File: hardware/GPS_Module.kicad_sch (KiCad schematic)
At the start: 1 part, among them U6 SAM-M8Q

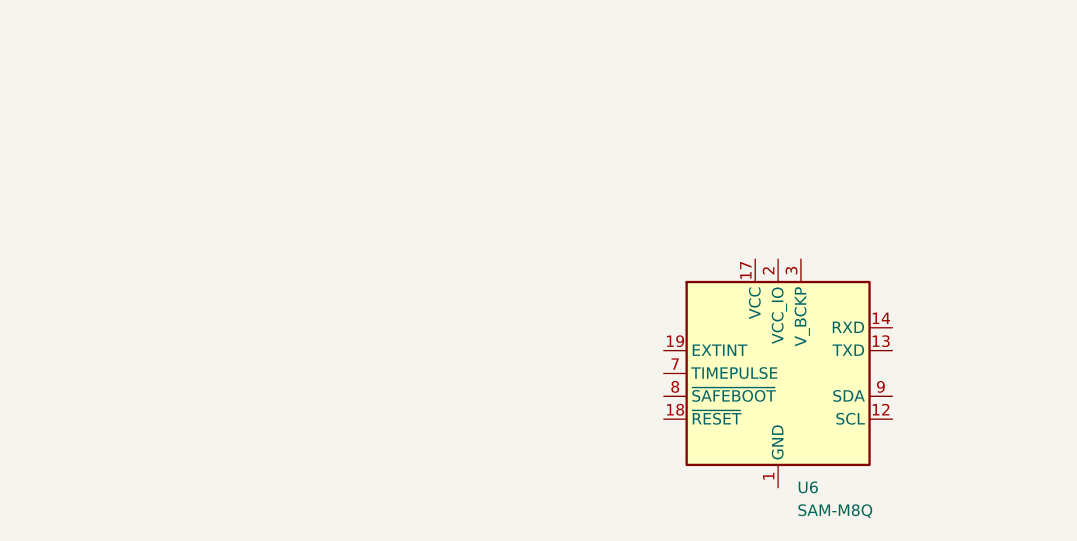
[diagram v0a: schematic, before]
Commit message: Main modules added + Com lines
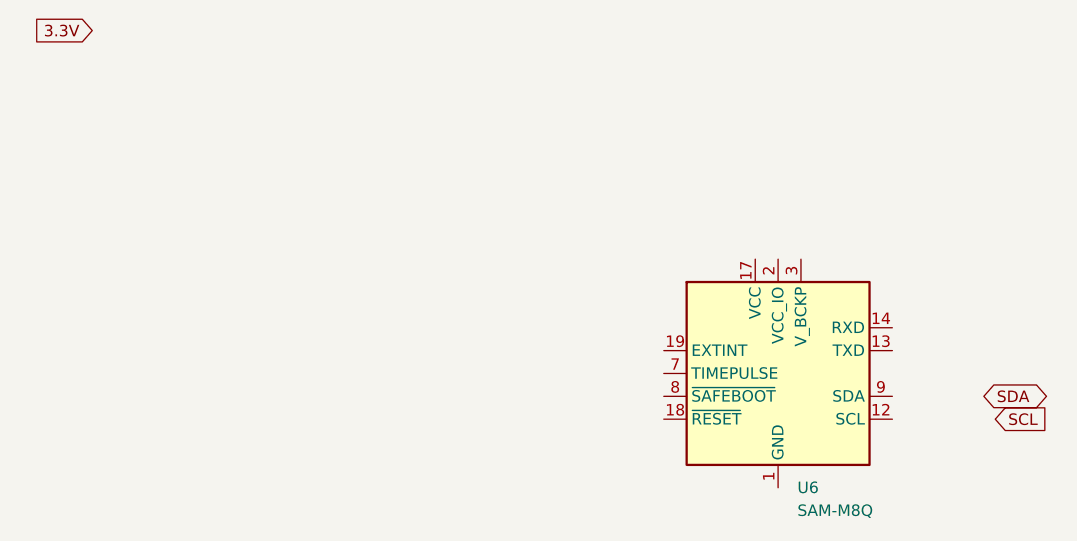
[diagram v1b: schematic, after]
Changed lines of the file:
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@@
 	(generator_version "9.0")
 	(paper "A4")
+	(global_label "3.3V"
+		(shape input)
+		(at 27.94 33.02 180)
+		(fields_autoplaced yes)
+		(effects
+			(font
+				(size 1.27 1.27)
+			)
+			(justify right)
+		)
+		(property "Intersheetrefs" "${INTERSHEET_REFS}"
+			(at 20.8424 33.02 0)
+			(effects
+				(font
+					(size 1.27 1.27)
+				)
+				(justify right)
+				(hide yes)
+			)
+		)
+	)
+	(global_label "SCL"
+		(shape input)
+		(at 128.27 76.2 0)
+		(fields_autoplaced yes)
+		(effects
+			(font
+				(size 1.27 1.27)
+			)
+			(justify left)
+		)
+		(property "Intersheetrefs" "${INTERSHEET_REFS}"
+			(at 134.7628 76.2 0)
+			(effects
+				(font
+					(size 1.27 1.27)
+				)
+				(justify left)
+				(hide yes)
+			)
+		)
+	)
+	(global_label "SDA"
+		(shape bidirectional)
+		(at 127 73.66 0)
+		(fields_autoplaced yes)
+		(effects
+			(font
+				(size 1.27 1.27)
+			)
+			(justify left)
+		)
+		(property "Intersheetrefs" "${INTERSHEET_REFS}"
+			(at 134.6646 73.66 0)
+			(effects
+				(font
+					(size 1.27 1.27)
+				)
+				(justify left)
+				(hide yes)
+			)
+		)
+	)
 	(symbol
 		(lib_id "RF_GPS:SAM-M8Q")

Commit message: GPS schematic + datasheet
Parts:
- added C10: 1µF, Capacitor_SMD:C_0603_1608Metric, symbol Device:C
- added D1: R_LED, LED_SMD:LED_0603_1608Metric, symbol Device:LED
- added J2, J3, J4: Conn_01x04_Pin, Connector_JST:JST_XA_B04B-XASK-1_1x04_P2.50mm_Vertical, symbol Connector:Conn_01x04_Pin
- added R13: 1k, Resistor_SMD:R_0603_1608Metric, symbol Device:R
- added R14, R15: 470, Resistor_SMD:R_0603_1608Metric, symbol Device:R
- added R8, R9: 22, Resistor_SMD:R_0603_1608Metric, symbol Device:R
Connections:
- net 3.3V: now also U6.17 (VCC), U6.2 (VCC_IO), C10.1, J2.1 (Pin_1), J3.1 (Pin_1)
- net SCL: now also J2.2 (Pin_2), R9.1
- net SDA: now also J2.3 (Pin_3), R8.2
- net GND: now reaches U6.1 (GND), U6.10 (GND), U6.11 (GND), U6.15 (GND), U6.16 (GND), U6.20 (GND), U6.4 (GND), U6.5 (GND), U6.6 (GND)
- net GND: now also C10.2, D1.1 (K), J2.4 (Pin_4), J3.4 (Pin_4)
- net at U6.12 (SCL): now also R9.2
- net at U6.13 (TXD): now also R15.2
- net at U6.14 (RXD): now also R14.1
- net ~{reset}: now reaches U6.18 (~{RESET})
- net ~{reset}: now also J4.4 (Pin_4)
- net EXTINT: now reaches U6.19 (EXTINT)
- net EXTINT: now also J4.1 (Pin_1)
- net TP: now reaches U6.7 (TIMEPULSE)
- net TP: now also J4.2 (Pin_2), R13.2
- net ~{safe}: now reaches U6.8 (~{SAFEBOOT})
- net ~{safe}: now also J4.3 (Pin_3)
- net at U6.9 (SDA): now also R8.1
- new net: D1.2 (A), R13.1
- new net RX_GPS: J3.3 (Pin_3), R14.2
- new net TX_GPS: J3.2 (Pin_2), R15.1
- no-connect marks 0 -> 1
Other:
- moved on the sheet: U6

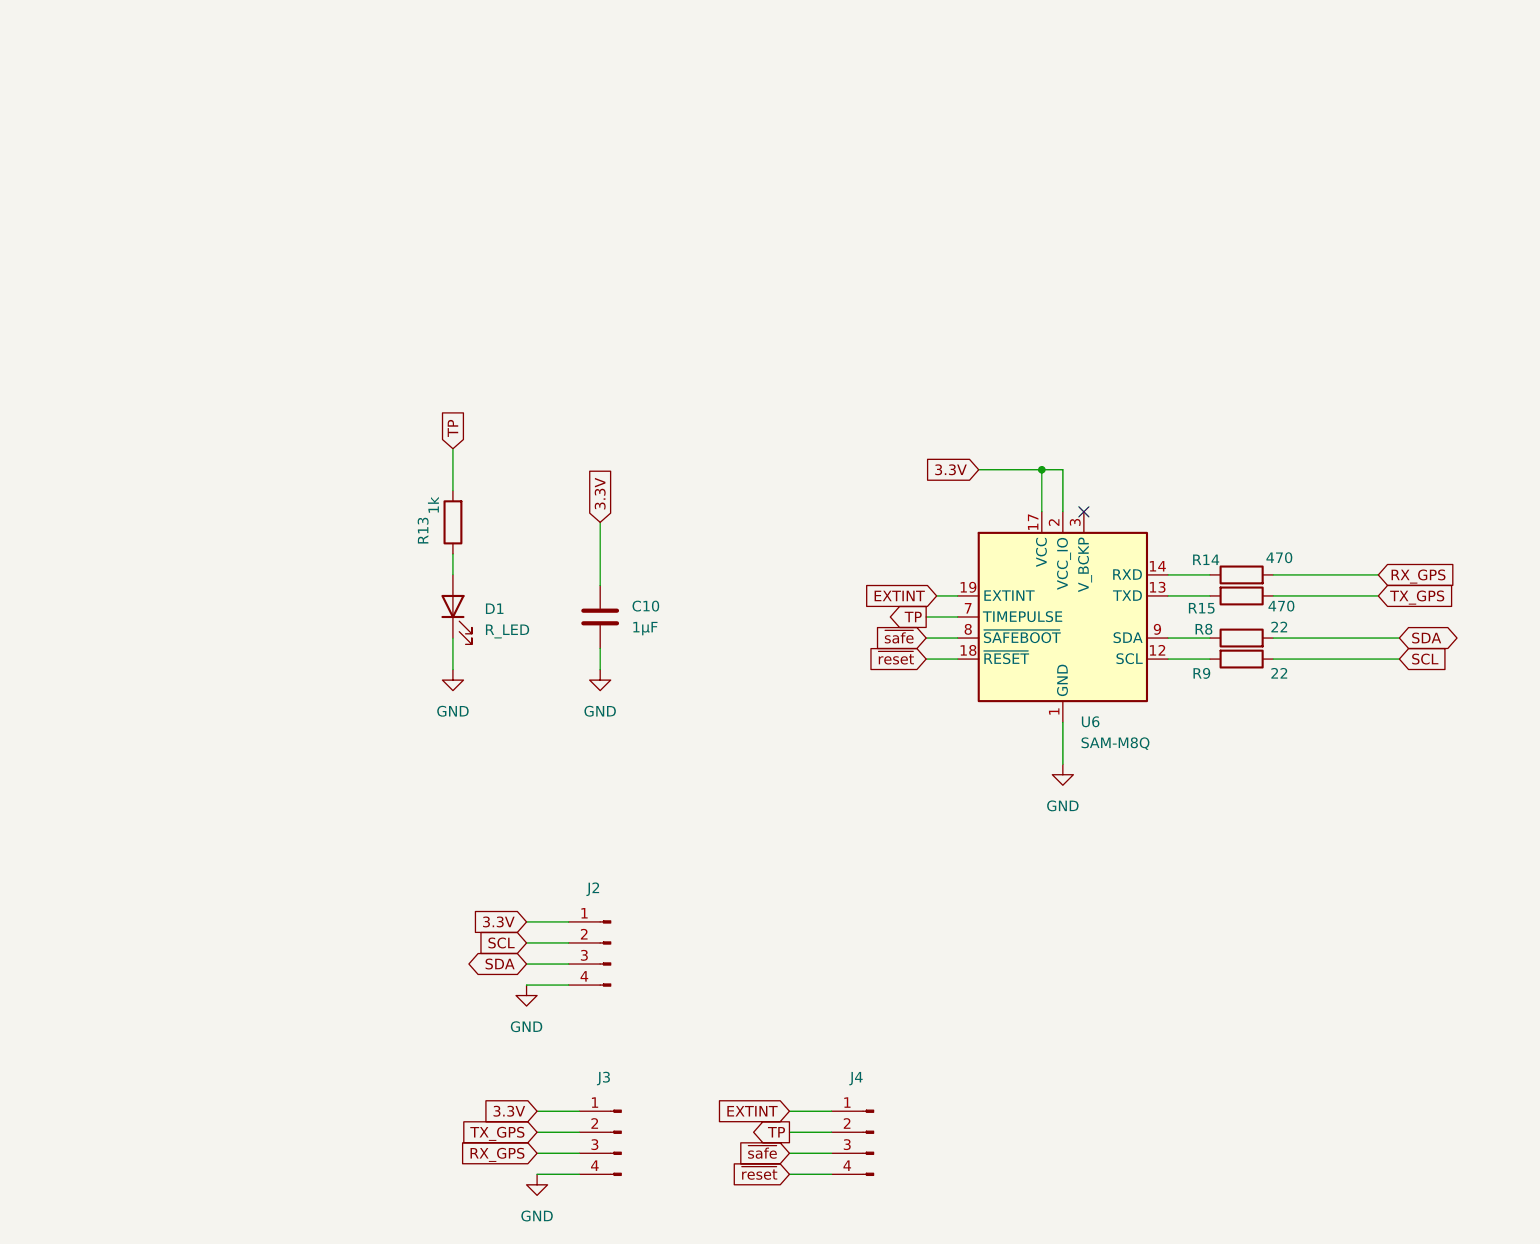
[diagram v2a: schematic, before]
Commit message: ESL protection modification with usblc6 2sc6
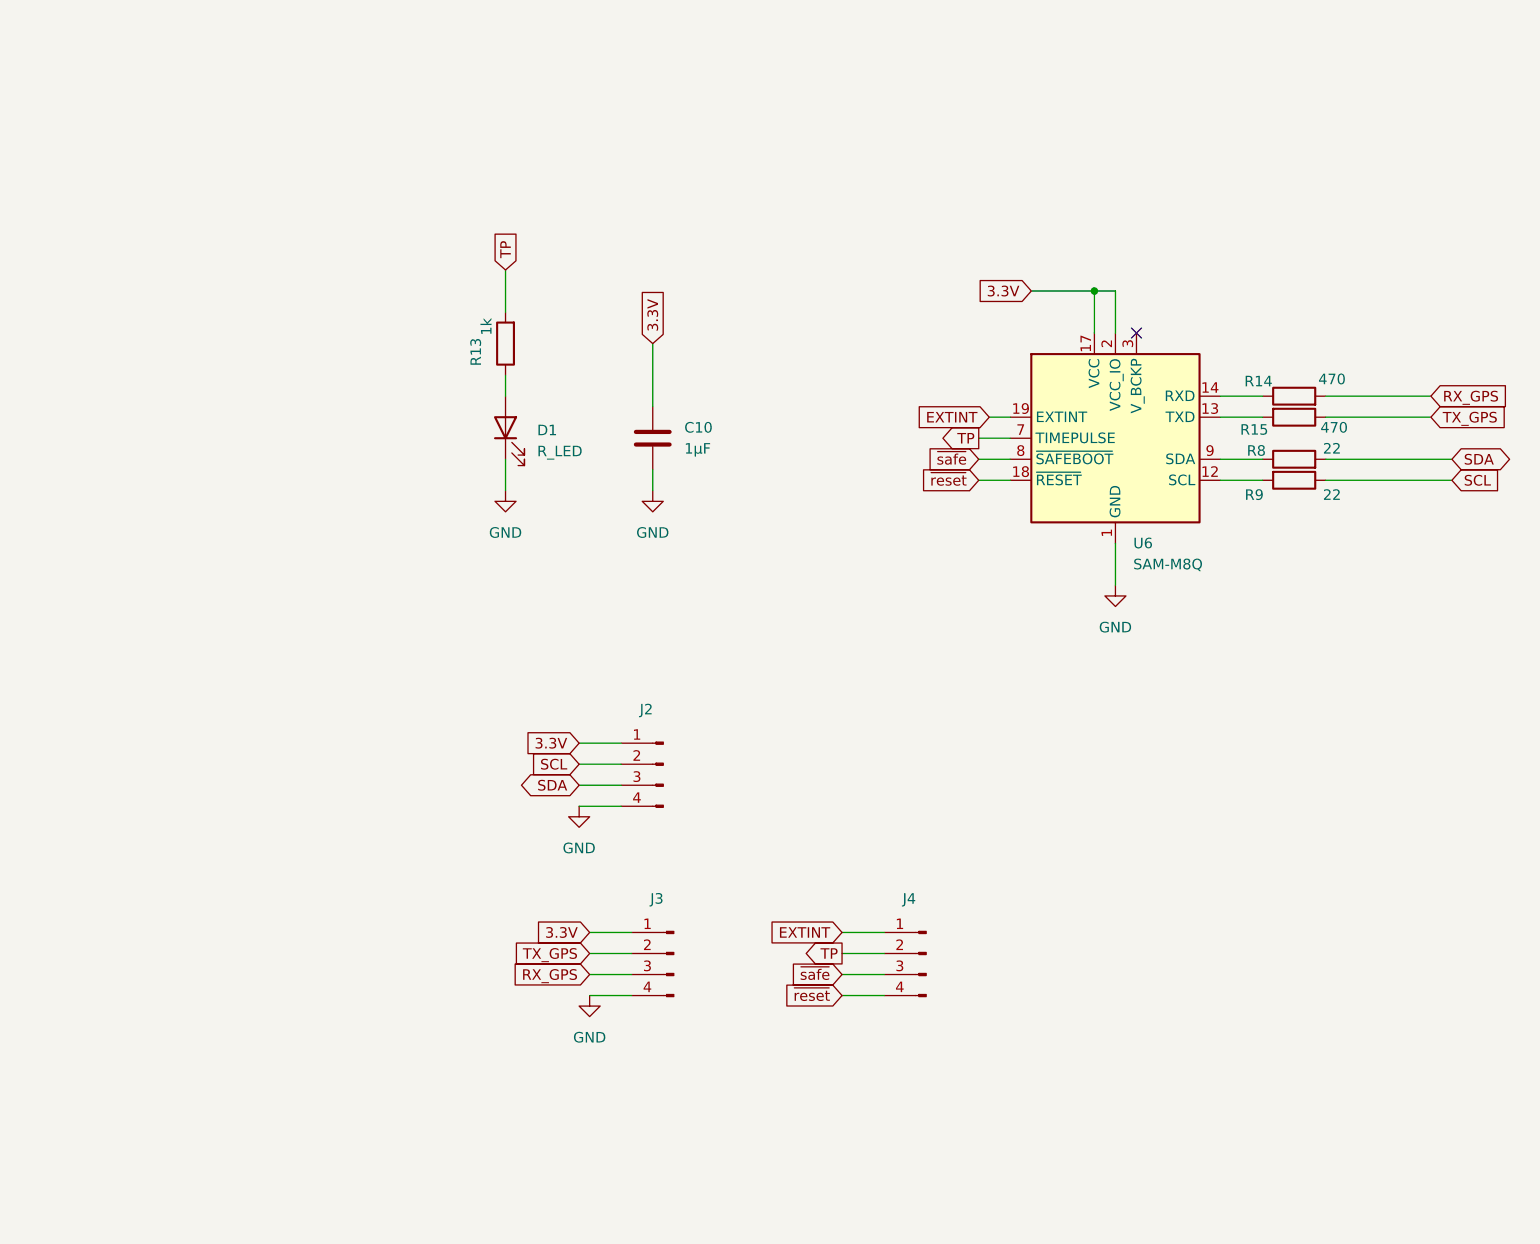
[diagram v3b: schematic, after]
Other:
- moved on the sheet: C10, D1, J2, J3, J4, R13, R14, R15, R8, R9, U6

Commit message: Found all diodes & transistors footprint & JLCPCB
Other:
- company: (none) -> ECAM Brussels Engineering School
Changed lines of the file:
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@@
 	(generator_version "9.0")
 	(paper "A4")
+	(title_block
+		(rev "0.1")
+		(company "ECAM Brussels Engineering School")
+	)
 	(junction
 		(at 149.86 64.77)

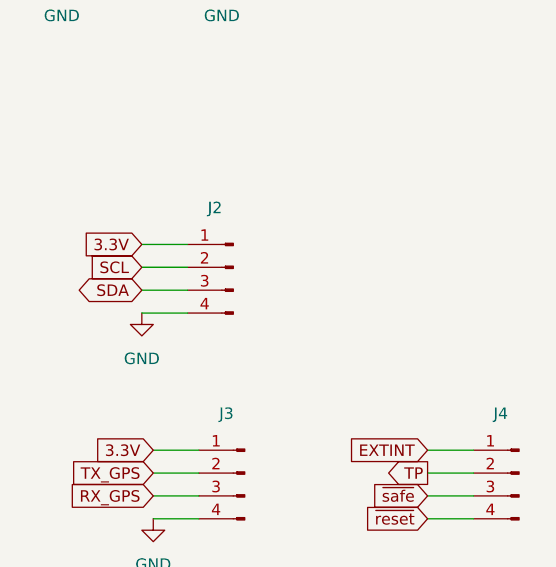
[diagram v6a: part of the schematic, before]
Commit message: Update ESP32 pins
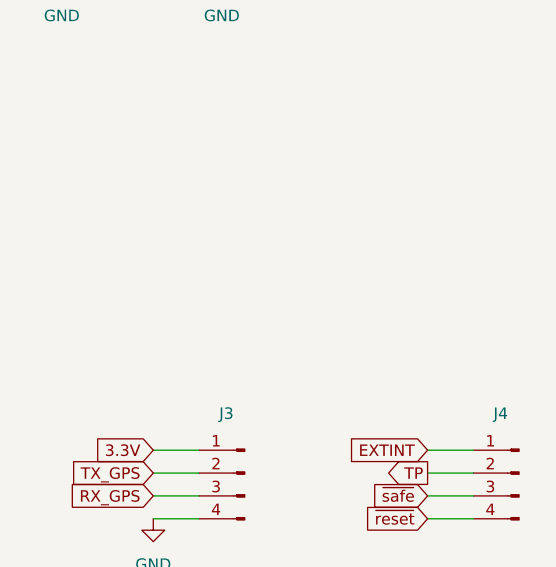
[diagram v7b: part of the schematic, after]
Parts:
- removed J2: Conn_01x04_Pin, Connector_JST:JST_XA_B04B-XASK-1_1x04_P2.50mm_Vertical, symbol Connector:Conn_01x04_Pin
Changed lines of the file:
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@@
-	(wire
-		(pts
-			(xy 87.63 119.38) (xy 92.71 119.38)
-		)
-		(stroke
-			(width 0)
-			(type default)
-		)
-	)
 	(wire
 		(pts
@@
 	(wire
 		(pts
-			(xy 87.63 121.92) (xy 92.71 121.92)
-		)
-		(stroke
-			(width 0)
-			(type default)
-		)
-	)
-	(wire
-		(pts
 			(xy 119.38 142.24) (xy 124.46 142.24)
 		)
@@
 	(wire
 		(pts
-			(xy 87.63 127) (xy 92.71 127)
-		)
-		(stroke
-			(width 0)
-			(type default)
-		)
-	)
-	(wire
-		(pts
 			(xy 88.9 147.32) (xy 93.98 147.32)
 		)
@@
 	(wire
 		(pts
-			(xy 87.63 124.46) (xy 92.71 124.46)
-		)
-		(stroke
-			(width 0)
-			(type default)
-		)
-	)
-	(wire
-		(pts
 			(xy 135.89 85.09) (xy 139.7 85.09)
 		)
@@
 				)
 				(justify left)
-				(hide yes)
-			)
-		)
-	)
-	(global_label "SCL"
-		(shape input)
-		(at 87.63 121.92 180)
-		(fields_autoplaced yes)
-		(effects
-			(font
-				(size 1.27 1.27)
-			)
-			(justify right)
-		)
-		(property "Intersheetrefs" "${INTERSHEET_REFS}"
-			(at 81.1372 121.92 0)
-			(effects
-				(font
-					(size 1.27 1.27)
-				)
-				(justify right)
 				(hide yes)
 			)
@@
 		)
 	)
-	(global_label "3.3V"
-		(shape input)
-		(at 87.63 119.38 180)
-		(fields_autoplaced yes)
-		(effects
-			(font
-				(size 1.27 1.27)
-			)
-			(justify right)
-		)
-		(property "Intersheetrefs" "${INTERSHEET_REFS}"
-			(at 80.5324 119.38 0)
-			(effects
-				(font
-					(size 1.27 1.27)
-				)
-				(justify right)
-				(hide yes)
-			)
-		)
-	)
 	(global_label "SCL"
 		(shape input)
@@
 		(property "Intersheetrefs" "${INTERSHEET_REFS}"
 			(at 114.1572 144.78 0)
-			(effects
-				(font
-					(size 1.27 1.27)
-				)
-				(justify right)
-				(hide yes)
-			)
-		)
-	)
-	(global_label "SDA"
-		(shape bidirectional)
-		(at 87.63 124.46 180)
-		(fields_autoplaced yes)
-		(effects
-			(font
-				(size 1.27 1.27)
-			)
-			(justify right)
-		)
-		(property "Intersheetrefs" "${INTERSHEET_REFS}"
-			(at 79.9654 124.46 0)
 			(effects
 				(font
@@
 					(unit 1)
 				)
-			)
-		)
-	)
-	(symbol
-		(lib_id "power:GND")
-		(at 87.63 127 0)
-		(unit 1)
-		(exclude_from_sim no)
-		(in_bom yes)
-		(on_board yes)
-		(dnp no)
-		(fields_autoplaced yes)
-		(property "Reference" "#PWR019"
-			(at 87.63 133.35 0)
-			(effects
-				(font
-					(size 1.27 1.27)
-				)
-				(hide yes)
-			)
-		)
-		(property "Value" "GND"
-			(at 87.63 132.08 0)
-			(effects
-				(font
-					(size 1.27 1.27)
-				)
-			)
-		)
-		(property "Footprint" ""
-			(at 87.63 127 0)
-			(effects
-				(font
-					(size 1.27 1.27)
-				)
-				(hide yes)
-			)
-		)
-		(property "Datasheet" ""
-			(at 87.63 127 0)
-			(effects
-				(font
-					(size 1.27 1.27)
-				)
-				(hide yes)
-			)
-		)
-		(property "Description" "Power symbol creates a global label with name \"GND\" , ground"
-			(at 87.63 127 0)
-			(effects
-				(font
-					(size 1.27 1.27)
-				)
-				(hide yes)
-			)
-		)
-		(pin "1"
-		)
-		(instances
-			(project "GOG"
-				(path "/5b969f6e-a36e-432b-8f00-b2d6a515a877/86749ea3-b799-4cf0-94d1-46de6ccb32b0"
-					(reference "#PWR019")
-					(unit 1)
-				)
-			)
-		)
-	)
-	(symbol
-		(lib_id "Connector:Conn_01x04_Pin")
-		(at 97.79 121.92 0)
-		(mirror y)
-		(unit 1)
-		(exclude_from_sim no)
-		(in_bom yes)
-		(on_board yes)
-		(dnp no)
-		(property "Reference" "J2"
-			(at 95.758 115.316 0)
-			(effects
-				(font
-					(size 1.27 1.27)
-				)
-			)
-		)
-		(property "Value" "Conn_01x04_Pin"
-			(at 97.155 116.84 0)
-			(effects
-				(font
-					(size 1.27 1.27)
-				)
-				(hide yes)
-			)
-		)
-		(property "Footprint" "Connector_JST:JST_XA_B04B-XASK-1_1x04_P2.50mm_Vertical"
-			(at 97.79 121.92 0)
-			(effects
-				(font
-					(size 1.27 1.27)
-				)
-				(hide yes)
-			)
-		)
-		(property "Datasheet" "~"
-			(at 97.79 121.92 0)
-			(effects
-				(font
-					(size 1.27 1.27)
-				)
-				(hide yes)
-			)
-		)
-		(property "Description" "Generic connector, single row, 01x04, script generated"
-			(at 97.79 121.92 0)
-			(effects
-				(font
-					(size 1.27 1.27)
-				)
-				(hide yes)
-			)
-		)
-		(pin "3"
-		)
-		(pin "2"
-		)
-		(pin "1"
-		)
-		(pin "4"
-		)
-		(instances
-			(project ""
-				(path "/5b969f6e-a36e-432b-8f00-b2d6a515a877/86749ea3-b799-4cf0-94d1-46de6ccb32b0"
-					(reference "J2")
-					(unit 1)
-				)
